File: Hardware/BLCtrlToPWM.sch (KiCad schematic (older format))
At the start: 39 parts, among them IC1 ATMEGA2560-A, Q1 Q_NMOS_GSD, Q2 Q_NMOS_GSD, Q3 Q_NMOS_GSD, Q4 Q_NMOS_GSD, Q5 Q_NMOS_GSD, SW1 SW_SPST, Y1 16MHz

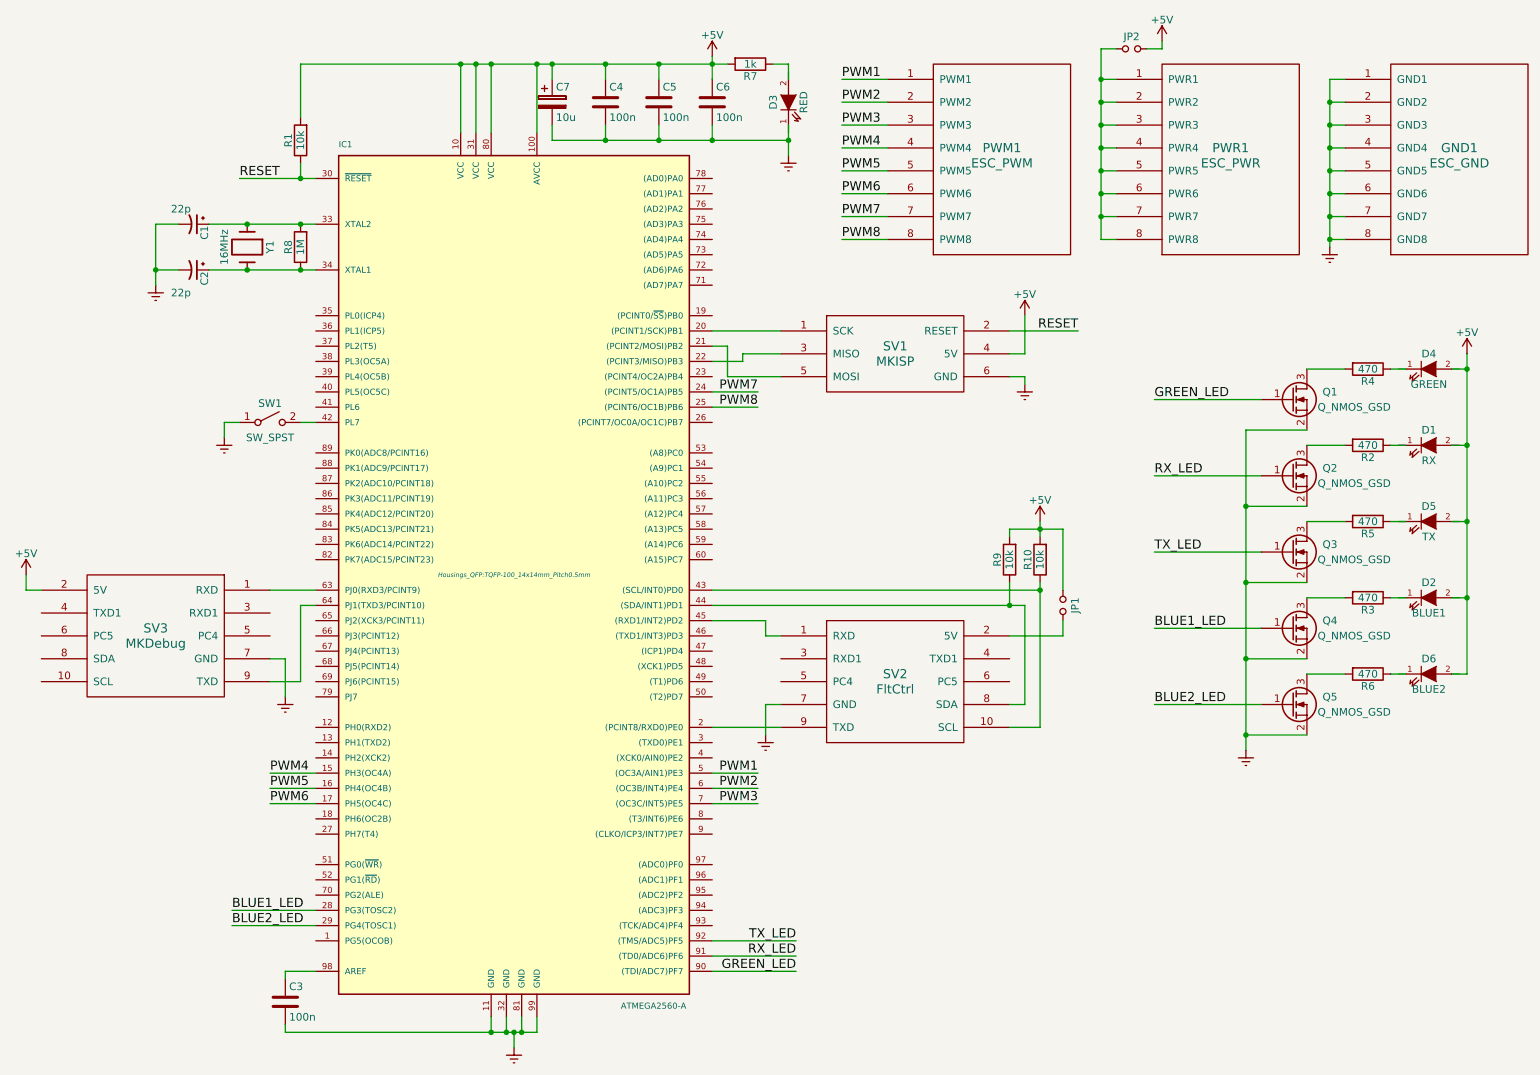
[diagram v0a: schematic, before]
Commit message: Updated resistor values and BOM
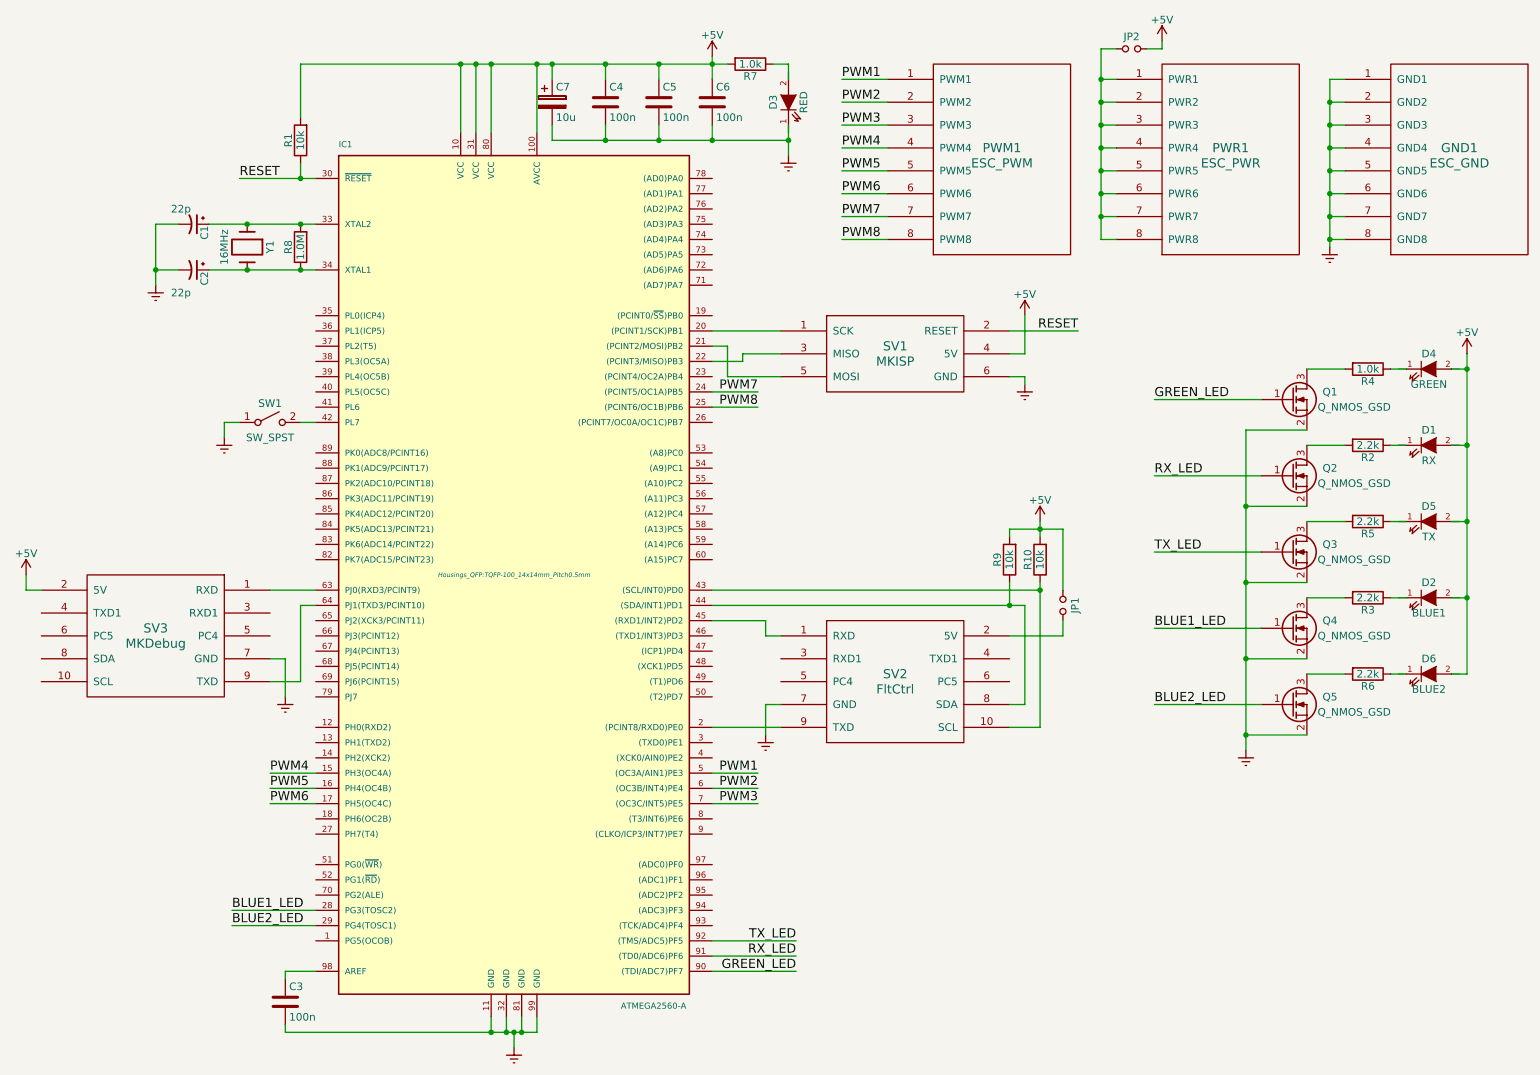
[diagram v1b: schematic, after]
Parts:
- R2, R3, R5, R6: value 470 -> 2.2k
- R4: value 470 -> 1.0k
- R7: value 1k -> 1.0k
- R8: value 1M -> 1.0M
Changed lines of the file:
@@
 P 5600 1000
 F 0 "R7" V 5680 1000 50  0000 C CNN
-F 1 "1k" V 5600 1000 50  0000 C CNN
+F 1 "1.0k" V 5600 1000 50  0000 C CNN
 F 2 "Resistors_SMD:R_0805_HandSoldering" V 5530 1000 30  0001 C CNN
 F 3 "" H 5600 1000 30  0000 C CNN
@@
 P 9650 3500
 F 0 "R2" V 9730 3500 50  0000 C CNN
-F 1 "470" V 9650 3500 50  0000 C CNN
+F 1 "2.2k" V 9650 3500 50  0000 C CNN
 F 2 "Resistors_SMD:R_0805_HandSoldering" V 9580 3500 30  0001 C CNN
 F 3 "" H 9650 3500 30  0000 C CNN
@@
 P 9650 3000
 F 0 "R4" V 9730 3000 50  0000 C CNN
-F 1 "470" V 9650 3000 50  0000 C CNN
+F 1 "1.0k" V 9650 3000 50  0000 C CNN
 F 2 "Resistors_SMD:R_0805_HandSoldering" V 9580 3000 30  0001 C CNN
 F 3 "" H 9650 3000 30  0000 C CNN
@@
 P 9650 4000
 F 0 "R5" V 9730 4000 50  0000 C CNN
-F 1 "470" V 9650 4000 50  0000 C CNN
+F 1 "2.2k" V 9650 4000 50  0000 C CNN
 F 2 "Resistors_SMD:R_0805_HandSoldering" V 9580 4000 30  0001 C CNN
 F 3 "" H 9650 4000 30  0000 C CNN
@@
 P 9650 4500
 F 0 "R3" V 9730 4500 50  0000 C CNN
-F 1 "470" V 9650 4500 50  0000 C CNN
+F 1 "2.2k" V 9650 4500 50  0000 C CNN
 F 2 "Resistors_SMD:R_0805_HandSoldering" V 9580 4500 30  0001 C CNN
 F 3 "" H 9650 4500 30  0000 C CNN
@@
 P 9650 5000
 F 0 "R6" V 9730 5000 50  0000 C CNN
-F 1 "470" V 9650 5000 50  0000 C CNN
+F 1 "2.2k" V 9650 5000 50  0000 C CNN
 F 2 "Resistors_SMD:R_0805_HandSoldering" V 9580 5000 30  0001 C CNN
 F 3 "" H 9650 5000 30  0000 C CNN
@@
 P 2650 2200
 F 0 "R8" V 2730 2200 50  0000 C CNN
-F 1 "1M" V 2650 2200 50  0000 C CNN
+F 1 "1.0M" V 2650 2200 50  0000 C CNN
 F 2 "Resistors_SMD:R_0805_HandSoldering" V 2580 2200 30  0001 C CNN
 F 3 "" H 2650 2200 30  0000 C CNN
